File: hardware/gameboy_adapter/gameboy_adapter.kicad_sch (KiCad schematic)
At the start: 3 parts, among them J1 CART SLOT TOP ROW, J2 GBA_Slot, SW1 SW_SPDT

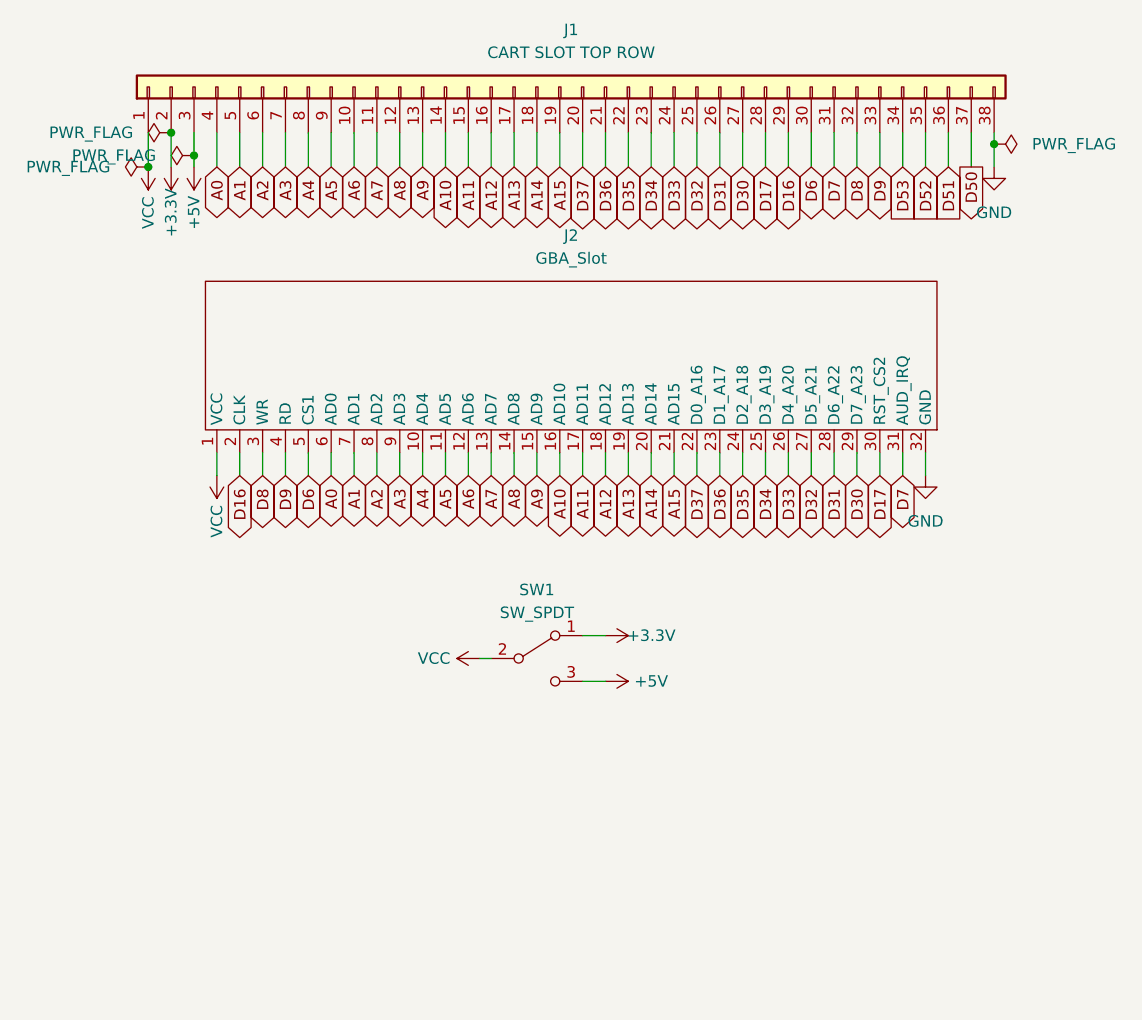
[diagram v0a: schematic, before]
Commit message: update schematic
relink GBA symbol; rename SPI pins on main header; relink footprints
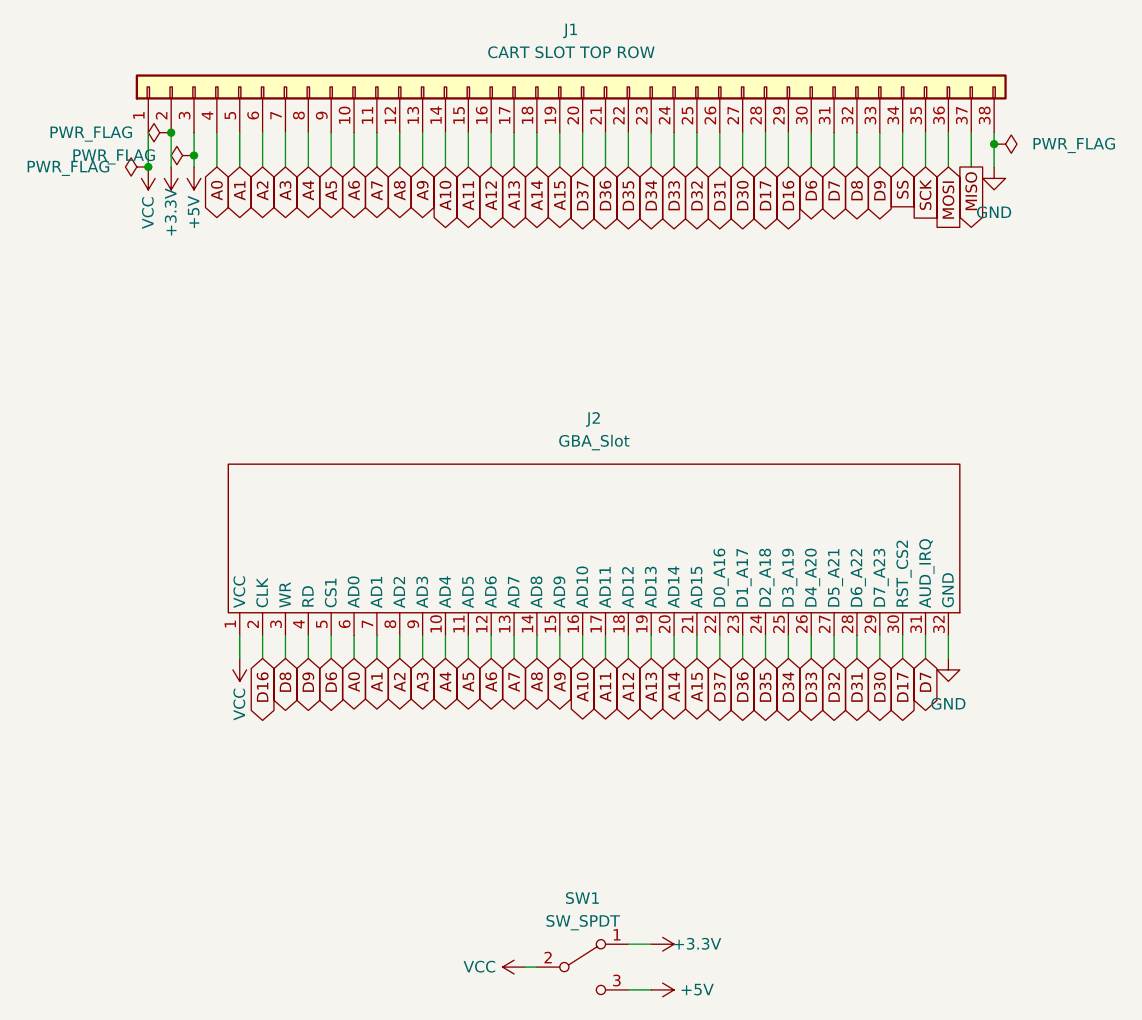
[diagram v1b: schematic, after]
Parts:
- J2: footprint (none) -> !OSCR:GBA_Slot; symbol sanni:GBA_Slot -> !OSCR:GBA_Slot
- SW1: footprint (none) -> Button_Switch_THT:SW_CuK_OS102011MA1QN1_SPDT_Angled
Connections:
- net +3V3 renamed +3.3V
- net D50 renamed MISO
- net D51 renamed MOSI
- net D52 renamed SCK
- net D53 renamed SS
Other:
- title: OSCR GAMEBOY ADAPTER -> OSCR GAMEBOY BREAKOUT
- moved on the sheet: J2, SW1

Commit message: change footprint of cart slot to pin header
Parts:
- J1: footprint Connector_PinSocket_2.54mm:PinSocket_1x38_P2.54mm_Vertical -> Connector_PinHeader_2.54mm:PinHeader_1x38_P2.54mm_Vertical
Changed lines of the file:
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@@
     (property "Reference" "J1" (id 0) (at 85.09 26.67 90))
     (property "Value" "CART SLOT TOP ROW" (id 1) (at 85.09 29.21 90))
-    (property "Footprint" "Connector_PinSocket_2.54mm:PinSocket_1x38_P2.54mm_Vertical" (id 2) (at 83.82 33.02 0)
+    (property "Footprint" "Connector_PinHeader_2.54mm:PinHeader_1x38_P2.54mm_Vertical" (id 2) (at 83.82 33.02 0)
       (effects (font (size 1.27 1.27)) hide)
     )
@@
     )
     (path "/7f6cd577-ef9e-42a4-adf6-7998d45df605"
-      (reference "J1") (unit 1) (value "CART SLOT TOP ROW") (footprint "Connector_PinSocket_2.54mm:PinSocket_1x38_P2.54mm_Vertical")
+      (reference "J1") (unit 1) (value "CART SLOT TOP ROW") (footprint "Connector_PinHeader_2.54mm:PinHeader_1x38_P2.54mm_Vertical")
     )
     (path "/93730f4d-f5ea-4311-bd16-a096e537871b"

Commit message: Update gb breakout
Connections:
- net +3.3V: now also SW1.3 (C); no longer SW1.1 (A)
- net +5V: now also SW1.1 (A); no longer SW1.3 (C)
- net GND: now also J2.33 (GND_PAD_1), J2.34 (GND_PAD_2)
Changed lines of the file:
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@@
   (junction (at 43.18 40.64) (diameter 0) (color 0 0 0 0)
   )
+  (junction (at 132.08 80.01) (diameter 0) (color 0 0 0 0)
+  )
+  (junction (at 132.08 95.25) (diameter 0) (color 0 0 0 0)
+  )
   (junction (at 40.64 38.1) (diameter 0) (color 0 0 0 0)
   )
   (junction (at 38.1 41.91) (diameter 0) (color 0 0 0 0)
   )
+  (wire (pts (xy 91.44 133.35) (xy 93.98 133.35))
+    (stroke (width 0) (type default) (color 0 0 0 0))
+  )
   (wire (pts (xy 101.6 93.98) (xy 101.6 96.52))
     (stroke (width 0) (type default) (color 0 0 0 0))
@@
     (stroke (width 0) (type default) (color 0 0 0 0))
   )
+  (wire (pts (xy 132.08 77.47) (xy 132.08 80.01))
+    (stroke (width 0) (type default) (color 0 0 0 0))
+  )
   (wire (pts (xy 78.74 93.98) (xy 78.74 96.52))
     (stroke (width 0) (type default) (color 0 0 0 0))
@@
     (stroke (width 0) (type default) (color 0 0 0 0))
   )
-  (wire (pts (xy 127 93.98) (xy 127 96.52))
+  (wire (pts (xy 91.44 128.27) (xy 93.98 128.27))
     (stroke (width 0) (type default) (color 0 0 0 0))
   )
@@
     (stroke (width 0) (type default) (color 0 0 0 0))
   )
+  (wire (pts (xy 127 95.25) (xy 132.08 95.25))
+    (stroke (width 0) (type default) (color 0 0 0 0))
+  )
   (wire (pts (xy 71.12 38.1) (xy 71.12 41.91))
     (stroke (width 0) (type default) (color 0 0 0 0))
@@
     (stroke (width 0) (type default) (color 0 0 0 0))
   )
-  (wire (pts (xy 91.44 133.35) (xy 93.98 133.35))
-    (stroke (width 0) (type default) (color 0 0 0 0))
-  )
   (wire (pts (xy 58.42 38.1) (xy 58.42 41.91))
     (stroke (width 0) (type default) (color 0 0 0 0))
@@
     (stroke (width 0) (type default) (color 0 0 0 0))
   )
+  (wire (pts (xy 130.81 80.01) (xy 132.08 80.01))
+    (stroke (width 0) (type default) (color 0 0 0 0))
+  )
   (wire (pts (xy 63.5 38.1) (xy 63.5 41.91))
     (stroke (width 0) (type default) (color 0 0 0 0))
@@
     (stroke (width 0) (type default) (color 0 0 0 0))
   )
+  (wire (pts (xy 132.08 95.25) (xy 132.08 96.52))
+    (stroke (width 0) (type default) (color 0 0 0 0))
+  )
   (wire (pts (xy 129.54 38.1) (xy 129.54 41.91))
     (stroke (width 0) (type default) (color 0 0 0 0))
@@
     (stroke (width 0) (type default) (color 0 0 0 0))
   )
+  (wire (pts (xy 127 93.98) (xy 127 95.25))
+    (stroke (width 0) (type default) (color 0 0 0 0))
+  )
   (wire (pts (xy 88.9 38.1) (xy 88.9 41.91))
     (stroke (width 0) (type default) (color 0 0 0 0))
@@
     (stroke (width 0) (type default) (color 0 0 0 0))
   )
+  (wire (pts (xy 132.08 80.01) (xy 132.08 95.25))
+    (stroke (width 0) (type default) (color 0 0 0 0))
+  )
   (wire (pts (xy 40.64 38.1) (xy 40.64 41.91))
     (stroke (width 0) (type default) (color 0 0 0 0))
@@
     (stroke (width 0) (type default) (color 0 0 0 0))
   )
-  (wire (pts (xy 91.44 128.27) (xy 93.98 128.27))
-    (stroke (width 0) (type default) (color 0 0 0 0))
-  )
   (wire (pts (xy 99.06 93.98) (xy 99.06 96.52))
     (stroke (width 0) (type default) (color 0 0 0 0))
@@
   )
   (wire (pts (xy 80.01 130.81) (xy 81.28 130.81))
+    (stroke (width 0) (type default) (color 0 0 0 0))
+  )
+  (wire (pts (xy 130.81 77.47) (xy 132.08 77.47))
     (stroke (width 0) (type default) (color 0 0 0 0))
   )
@@
     (pin "1")
   )
-  (symbol (lib_id "power:+5V") (at 93.98 133.35 270) (unit 1)
+  (symbol (lib_id "power:+5V") (at 93.98 128.27 270) (unit 1)
     (in_bom yes) (on_board yes)
-    (property "Reference" "#PWR07" (id 0) (at 90.17 133.35 0)
-      (effects (font (size 1.27 1.27)) hide)
-    )
-    (property "Value" "+5V" (id 1) (at 99.06 133.35 90))
-    (property "Footprint" "" (id 2) (at 93.98 133.35 0)
-      (effects (font (size 1.27 1.27)) hide)
-    )
-    (property "Datasheet" "" (id 3) (at 93.98 133.35 0)
+    (property "Reference" "#PWR07" (id 0) (at 90.17 128.27 0)
+      (effects (font (size 1.27 1.27)) hide)
+    )
+    (property "Value" "+5V" (id 1) (at 99.06 128.27 90))
+    (property "Footprint" "" (id 2) (at 93.98 128.27 0)
+      (effects (font (size 1.27 1.27)) hide)
+    )
+    (property "Datasheet" "" (id 3) (at 93.98 128.27 0)
       (effects (font (size 1.27 1.27)) hide)
     )
@@
     (pin "3")
   )
-  (symbol (lib_id "power:+3.3V") (at 93.98 128.27 270) (unit 1)
+  (symbol (lib_id "power:+3.3V") (at 93.98 133.35 270) (unit 1)
     (in_bom yes) (on_board yes)
-    (property "Reference" "#PWR06" (id 0) (at 90.17 128.27 0)
-      (effects (font (size 1.27 1.27)) hide)
-    )
-    (property "Value" "+3.3V" (id 1) (at 99.06 128.27 90))
-    (property "Footprint" "" (id 2) (at 93.98 128.27 0)
-      (effects (font (size 1.27 1.27)) hide)
-    )
-    (property "Datasheet" "" (id 3) (at 93.98 128.27 0)
+    (property "Reference" "#PWR06" (id 0) (at 90.17 133.35 0)
+      (effects (font (size 1.27 1.27)) hide)
+    )
+    (property "Value" "+3.3V" (id 1) (at 99.06 133.35 90))
+    (property "Footprint" "" (id 2) (at 93.98 133.35 0)
+      (effects (font (size 1.27 1.27)) hide)
+    )
+    (property "Datasheet" "" (id 3) (at 93.98 133.35 0)
       (effects (font (size 1.27 1.27)) hide)
     )
@@
     (pin "31")
     (pin "32")
+    (pin "33")
+    (pin "34")
     (pin "4")
     (pin "5")
@@
     (pin "9")
   )
-  (symbol (lib_id "power:GND") (at 127 96.52 0) (unit 1)
+  (symbol (lib_id "power:GND") (at 132.08 96.52 0) (unit 1)
     (in_bom yes) (on_board yes) (fields_autoplaced)
-    (property "Reference" "#PWR08" (id 0) (at 127 102.87 0)
-      (effects (font (size 1.27 1.27)) hide)
-    )
-    (property "Value" "GND" (id 1) (at 127 101.6 0))
-    (property "Footprint" "" (id 2) (at 127 96.52 0)
-      (effects (font (size 1.27 1.27)) hide)
-    )
-    (property "Datasheet" "" (id 3) (at 127 96.52 0)
-      (effects (font (size 1.27 1.27)) hide)
-    )
+    (property "Reference" "#PWR08" (id 0) (at 132.08 102.87 0)
+      (effects (font (size 1.27 1.27)) hide)
+    )
+    (property "Value" "GND" (id 1) (at 132.08 101.6 0))
+    (property "Footprint" "" (id 2) (at 132.08 96.52 0)
+      (effects (font (size 1.27 1.27)) hide)
+    )
+    (property "Datasheet" "" (id 3) (at 132.08 96.52 0)
+      (effects (font (size 1.27 1.27)) hide)
+    )
